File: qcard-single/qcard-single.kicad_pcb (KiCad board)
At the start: 4 copper layers, 55 x 33.1 mm, 6 parts, among them J1 QCard_Conn, U1 SST39SF040

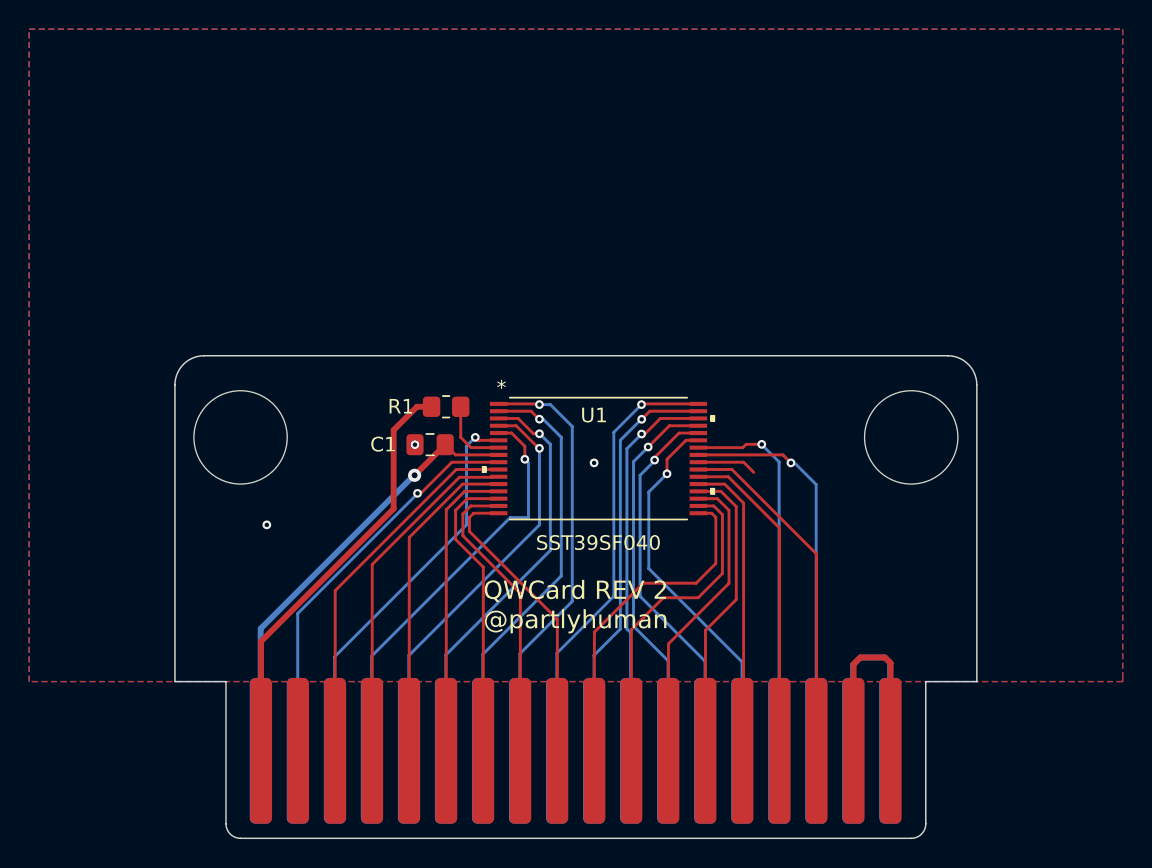
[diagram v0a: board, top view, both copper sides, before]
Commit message: Replace qcard-tsop32
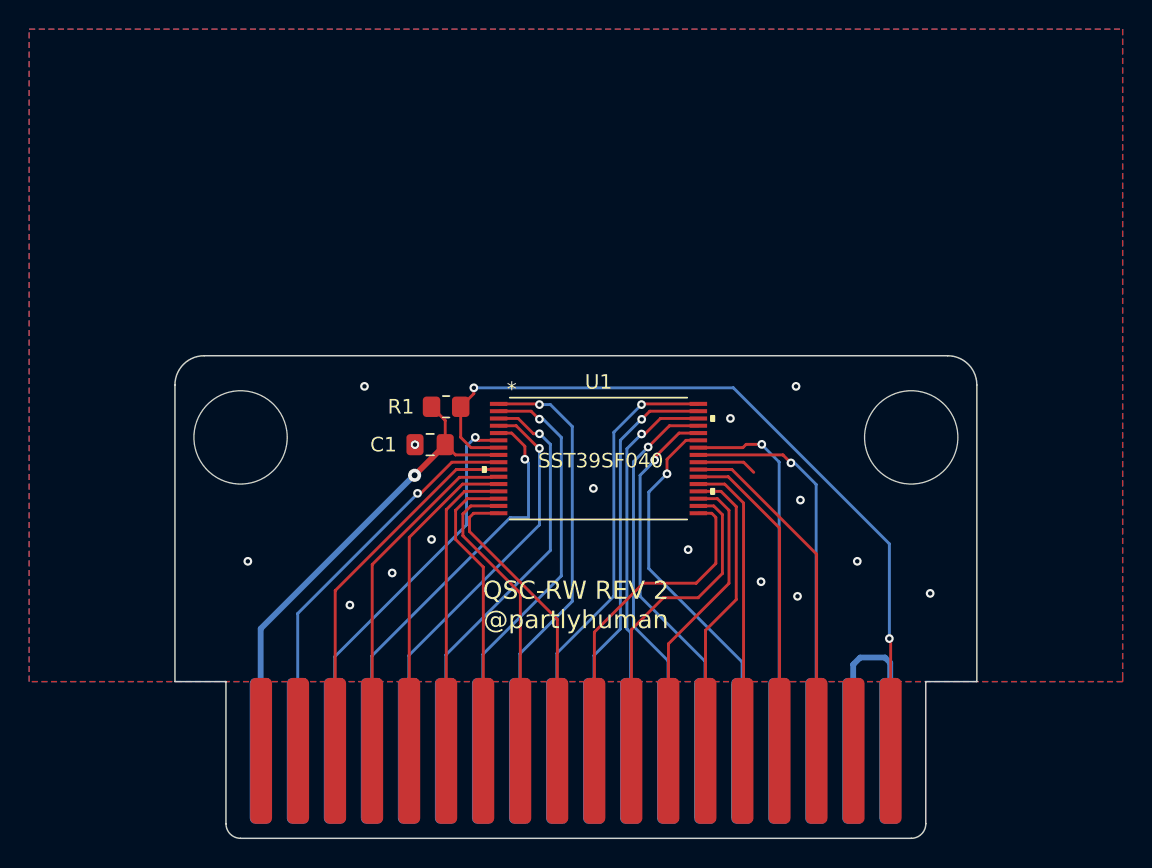
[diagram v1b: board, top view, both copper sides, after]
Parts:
- R1: value 1K -> 10K
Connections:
- J1 pad 2: /VCC_OR_WE -> GND
- J1 pad 36: GND -> Net-(J1-Pin_36)
- J1 pad 4: unconnected-(J1-Pin_4-Pad4) -> GND
- R1 pad 1: /VCC_OR_WE -> VCC
- R1 pad 2: Net-(U1-*WE) -> Net-(J1-Pin_36)
- U1 pad 7: Net-(U1-*WE) -> Net-(J1-Pin_36)
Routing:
- net Net-(J1-Pin_36): track 0.00 -> 53.8 mm, vias 0 -> 2
- net /VCC_OR_WE: track 29.0 -> 0.00 mm
- net GND: track 33.8 -> 18.9 mm, vias 3 -> 15
- net Net-(U1-*WE): track 4.99 -> 0.00 mm
- net VCC: track 30.2 -> 33.2 mm
